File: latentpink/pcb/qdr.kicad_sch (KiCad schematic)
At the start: 2 parts, among them U2 XC7K160T-2FBG484C, U3 CY7C2245KV18-450BZXI

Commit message: Continued initial schematic capture
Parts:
- added C124, C125, C126, C127: 4.7 uF, azonenberg_pcb:EIA_0603_CAP_NOSILK, symbol device:C
- added C128, C129, C130, C131, C132, C133, C134, C135, C136, C137, C138, C139, C140, C141, C142, C143, C144, C145, C146, C147, C148, C149, C150, C151, C152, C153: 0.47 uF, azonenberg_pcb:EIA_0402_CAP_NOSILK, symbol device:C
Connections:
- net GND: now reaches U3.C4 (GND)
- net GND: now also U3.C8 (GND), U3.D4 (GND), U3.D5 (GND), U3.D6 (GND), U3.D7 (GND), U3.D8 (GND), U3.E5 (GND), U3.E6 (GND), U3.E7 (GND), U3.F6 (GND), U3.G6 (GND), U3.H6 (GND), U3.J6 (GND), U3.K6 (GND), U3.L5 (GND), U3.L6 (GND), U3.L7 (GND), U3.M4 (GND), U3.M5 (GND), U3.M6 (GND), U3.M7 (GND), U3.M8 (GND), U3.N4 (GND), U3.N8 (GND), C124.2, C125.2, C126.2, C127.2, C128.2, C129.2, C130.2, C131.2, C132.2, C133.2, C134.2, C135.2, C136.2, C137.2, C138.2, C139.2, C140.2, C141.2, C142.2, C143.2, C144.2, C145.2, C146.2, C147.2, C148.2, C149.2, C150.2, C151.2, C152.2, C153.2
- net 1V8_IO: now reaches U3.E4 (VDDQ)
- net 1V8_IO: now also U3.E8 (VDDQ), U3.F4 (VDDQ), U3.F8 (VDDQ), U3.G4 (VDDQ), U3.G8 (VDDQ), U3.H3 (VDDQ), U3.H4 (VDDQ), U3.H8 (VDDQ), U3.H9 (VDDQ), U3.J4 (VDDQ), U3.J8 (VDDQ), U3.K4 (VDDQ), U3.K8 (VDDQ), U3.L4 (VDDQ), U3.L8 (VDDQ), C126.1, C127.1, C128.1, C131.1, C132.1, C133.1, C136.1, C137.1, C138.1, C141.1, C142.1, C143.1, C146.1, C147.1, C148.1, C151.1, C152.1, C153.1
- net 1V8: now reaches U3.F5 (VDD)
- net 1V8: now also U3.F7 (VDD), U3.G5 (VDD), U3.G7 (VDD), U3.H5 (VDD), U3.H7 (VDD), U3.J5 (VDD), U3.J7 (VDD), U3.K5 (VDD), U3.K7 (VDD), C124.1, C125.1, C129.1, C130.1, C134.1, C135.1, C139.1, C140.1, C144.1, C145.1, C149.1, C150.1
- net QDR_WPS_N: now reaches U3.A4 (WPS_N)
- net QDR_WPS_N: now also U2.K16 (IO_0_14)
- net QDR_BWS_2_N: now reaches U3.A5 (BWS_2_N)
- net QDR_BWS_2_N: now also U2.AA15 (IO_L18N_T2_13)
- net QDR_BWS_1_N: now reaches U3.A7 (BWS_1_N)
- net QDR_BWS_1_N: now also U2.W19 (IO_12N_T1_MRCC_13)
- net QDR_D18: now reaches U3.B3 (D18)
- net QDR_D18: now also U2.Y18 (IO_L13P_T2_MRCC_13)
- net QDR_BWS_3_N: now reaches U3.B5 (BWS_3_N)
- net QDR_BWS_3_N: now also U2.U15 (IO_L24N_T3_13)
- net QDR_BWS_0_N: now reaches U3.B7 (BWS_0_N)
- net QDR_BWS_0_N: now also U2.U20 (IO_L6N_T0_VREF_13)
- net QDR_D17: now reaches U3.B9 (D17)
- net QDR_D17: now also U2.V19 (IO_L12P_T1_MRCC_13)
- net QDR_D27: now reaches U3.C1 (D27)
- net QDR_D27: now also U2.U16 (IO_L19P_T3_13)
- net QDR_D8: now reaches U3.C11 (D8)
- net QDR_D8: now also U2.T20 (IO_L6P_T0_13)
- net QDR_D19: now reaches U3.C3 (D19)
- net QDR_D19: now also U2.Y19 (IO_L13N_T2_MRCC_13)
- net QDR_D16: now reaches U3.C9 (D16)
- net QDR_D16: now also U2.W20 (IO_L11N_T1_SRCC_13)
- net QDR_D28: now reaches U3.D1 (D28)
- net QDR_D28: now also U2.V17 (IO_L19N_T3_VREF_13)
- net QDR_D15: now reaches U3.D10 (D15)
- net QDR_D15: now also U2.V20 (IO_L11P_T1_SRCC_13)
- net QDR_D7: now reaches U3.D11 (D7)
- net QDR_D7: now also U2.V18 (IO_L5N_T0_13)
- net QDR_D20: now reaches U3.D2 (D20)
- net QDR_D20: now also U2.W17 (IO_L14P_T2_SRCC_13)
- net QDR_D6: now reaches U3.E10 (D6)
- net QDR_D6: now also U2.U17 (IO_L5P_T0_13)
- net QDR_D29: now reaches U3.E2 (D29)
- net QDR_D29: now also U2.R16 (IO_L20P_T3_13)
- net QDR_D21: now reaches U3.F3 (D21)
- net QDR_D21: now also U2.Y17 (IO_L14N_T2_SRCC_13)
- net QDR_D14: now reaches U3.F9 (D14)
- net QDR_D14: now also U2.AB20 (IO_L10N_T1_13)
- net QDR_D30: now reaches U3.G1 (D30)
- net QDR_D30: now also U2.T16 (IO_L20N_T3_13)
- net QDR_D13: now reaches U3.G10 (D13)
- net QDR_D13: now also U2.AA19 (IO_L10_PT1_13)
- net QDR_D5: now reaches U3.G11 (D5)
- net QDR_D5: now also U2.W22 (IO_L4N_T0_13)
- net QDR_D22: now reaches U3.G2 (D22)
- net QDR_D22: now also U2.AB15 (IO_L16P_T2_13)
- net QDR_D31: now reaches U3.J1 (D31)
- net QDR_D31: now also U2.W14 (IO_L22P_T3_13)
- net QDR_D4: now reaches U3.J11 (D4)
- net QDR_D4: now also U2.W21 (IO_L4P_T0_13)
- net QDR_D23: now reaches U3.J3 (D23)
- net QDR_D23: now also U2.AB16 (IO_L16N_T2_13)
- net QDR_D12: now reaches U3.J9 (D12)
- net QDR_D12: now also U2.AB21 (IO_L8N_T1_13)
- net QDR_D3: now reaches U3.K10 (D3)
- net QDR_D3: now also U2.V22 (IO_L2N_T0_13)
- net QDR_D32: now reaches U3.K2 (D32)
- net QDR_D32: now also U2.Y14 (IO_L22N_T3_13)
- net QDR_D24: now reaches U3.L3 (D24)
- net QDR_D24: now also U2.AA16 (IO_L17P_T2_13)
- net QDR_D11: now reaches U3.L9 (D11)
- net QDR_D11: now also U2.AA20 (IO_L8P_T1_13)
- net QDR_D33: now reaches U3.M1 (D33)
- net QDR_D33: now also U2.V15 (IO_L23P_T3_13)
- net QDR_D2: now reaches U3.M11 (D2)
- net QDR_D2: now also U2.U22 (IO_L2P_T0_13)
- net QDR_D25: now reaches U3.M3 (D25)
- net QDR_D25: now also U2.AB17 (IO_L17N_T2_13)
- net QDR_D10: now reaches U3.M9 (D10)
- net QDR_D10: now also U2.Y22 (IO_L7N_T1_13)
- net QDR_D34: now reaches U3.N1 (D34)
- net QDR_D34: now also U2.W15 (IO_L23N_T3_13)
- net QDR_D9: now reaches U3.N10 (D9)
- net QDR_D9: now also U2.Y21 (IO_L7P_T1_13)
- net QDR_D1: now reaches U3.N11 (D1)
- net QDR_D1: now also U2.U21 (IO_L1N_T0_13)
- net QDR_D26: now reaches U3.N2 (D26)
- net QDR_D26: now also U2.AA14 (IO_L18P_T2_13)
- net QDR_D0: now reaches U3.P10 (D0)
- net QDR_D0: now also U2.T21 (IO_L1P_T0_13)
- net QDR_D35: now reaches U3.P2 (D35)
- net QDR_D35: now also U2.T15 (IO_L24P_T3_13)
- net QDR_CQ_N: now reaches U3.A1 (CQ_N)
- net QDR_CQ_N: now also U2.L20 (IO_L12N_T1_MRCC_14)
- net QDR_CQ_P: now reaches U3.A11 (CQ_P)
- net QDR_CQ_P: now also U2.L19 (IO_L12P_T1_MRCC_14)
- net QDR_RPS_N: now reaches U3.A8 (RPS_N)
- net QDR_RPS_N: now also U2.H18 (IO_L1P_T0_D00_MOSI_14)
- net QDR_QVLD: now reaches U3.P6 (QVLD)
- net QDR_QVLD: now also U2.H19 (IO_L1N_T0_D01_DIN_14)
- net QDR_A10: now reaches U2.E21 (IO_L7P_T1_D09_14)
- net QDR_A10: now also U3.P7 (A)
- net QDR_A11: now reaches U2.E22 (IO_L7N_T1_D10_14)
- net QDR_A11: now also U3.P8 (A)
- net QDR_A1: now reaches U2.F19 (IO_L2N_T0_D03_14)
- net QDR_A1: now also U3.B4 (A)
- net QDR_A5: now reaches U2.F20 (IO_L4N_T0_D05_14)
- net QDR_A5: now also U3.N5 (A)
- net QDR_A15: now reaches U2.F21 (IO_L9N_T1_DQS_D13_14)
- net QDR_A15: now also U3.R7 (A)
- net QDR_A0: now reaches U2.G18 (IO_L2P_T0_D02_14)
- net QDR_A0: now also U3.A9 (A)
- net QDR_A4: now reaches U2.G20 (IO_L4P_T0_D04_14)
- net QDR_A4: now also U3.C7 (A)
- net QDR_A14: now reaches U2.G21 (IO_L9P_T1_DQS_14)
- net QDR_A14: now also U3.R5 (A)
- net QDR_A13: now reaches U2.G22 (IO_L8N_T1_D12_14)
- net QDR_A13: now also U3.R4 (A)
- net QDR_A12: now reaches U2.H22 (IO_L8P_T1_D11_14)
- net QDR_A12: now also U3.R3 (A)
- net QDR_A3: now reaches U2.J19 (IO_L3N_T0_DQS_EMCCLK_14)
- net QDR_A3: now also U3.C5 (A)
- net QDR_A16: now reaches U2.J21 (IO_L10P_T1_D14_14)
- net QDR_A16: now also U3.R8 (A)
- net QDR_A17: now reaches U2.J22 (IO_L10N_T1_D15_14)
- net QDR_A17: now also U3.R9 (A)
- net QDR_A9: now reaches U2.K17 (IO_L6N_T0_D08_VREF_14)
- net QDR_A9: now also U3.P5 (A)
- net QDR_A2: now reaches U2.K18 (IO_L3P_T0_DQS_PUDC_B_14)
- net QDR_A2: now also U3.B8 (A)
- net QDR_A7: now reaches U2.K19 (IO_L5N_T0_D07_14)
- net QDR_A7: now also U3.N7 (A)
- net QDR_A8: now reaches U2.L16 (IO_L6P_T0_FCS_B_14)
- net QDR_A8: now also U3.P4 (A)
- net QDR_A6: now reaches U2.L18 (IO_L5P_T0_D06_14)
- net QDR_A6: now also U3.N6 (A)
- net QDR_A20: now reaches U2.M17 (IO_L14P_T2_SRCC_14)
- net QDR_A20: now also U3.A2 (NC/288M)
- net QDR_A19: now reaches U2.M18 (IO_L14N_T2_SRCC_14)
- net QDR_A19: now also U3.A10 (NC/144M)
- net QDR_SYSCLK_P: now reaches U2.N18 (IO_L13P_T2_MRCC_14)
- net QDR_SYSCLK_N: now reaches U2.N19 (IO_L13N_T2_MRCC_14)
- net QDR_A18: now reaches U2.N22 (IO_L15P_T2_DQS_RDWR_B_14)
- net QDR_A18: now also U3.A3 (NC/72M)
- net QDR_K_P: now reaches U2.AA21 (IO_L9P_T1_DQS_13)
- net QDR_K_P: now also U3.B6 (K)
- net QDR_K_N: now reaches U2.AB22 (IO_L9N_T1_DQS_13)
- net QDR_K_N: now also U3.A6 (K_N)
- no-connect marks 0 -> 8
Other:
- note added: "TODO: verify termination * C/A bus: external resistors to Vtt * D: ODT on QDR * Q: DCI inputs on FPGA"
- moved on the sheet: U2C, U2D, U2E, U3B, U3C

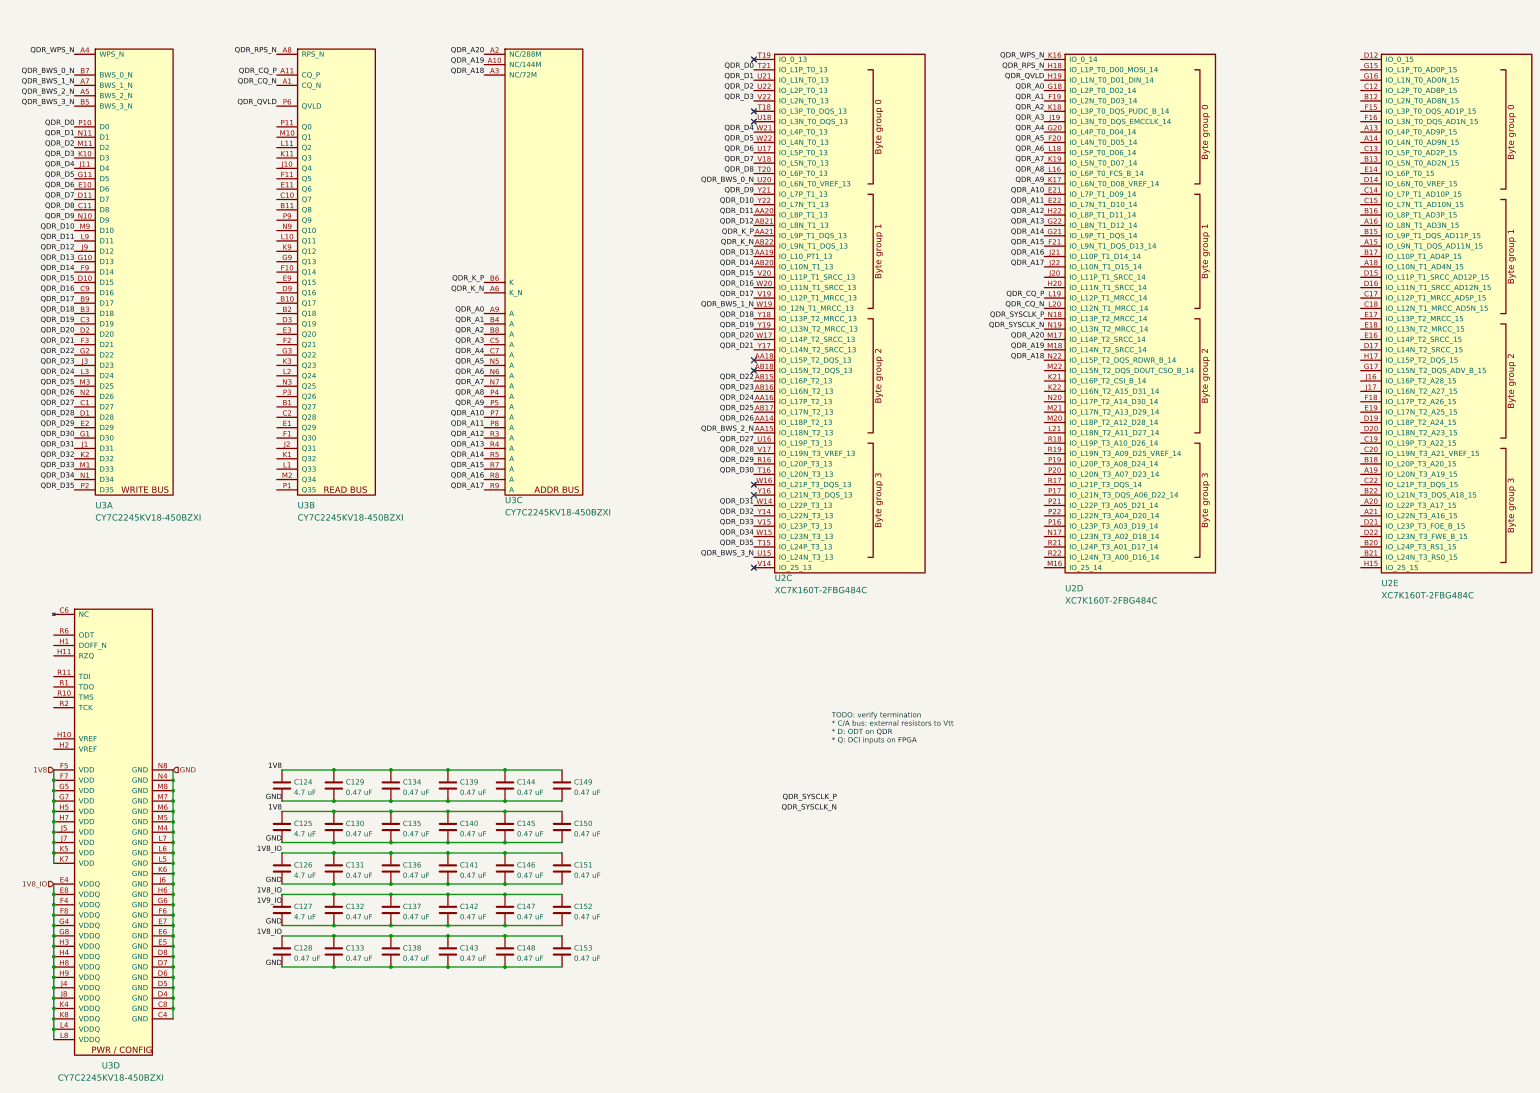
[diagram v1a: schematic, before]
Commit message: Continued work on schematic, mostly power supply and QDR
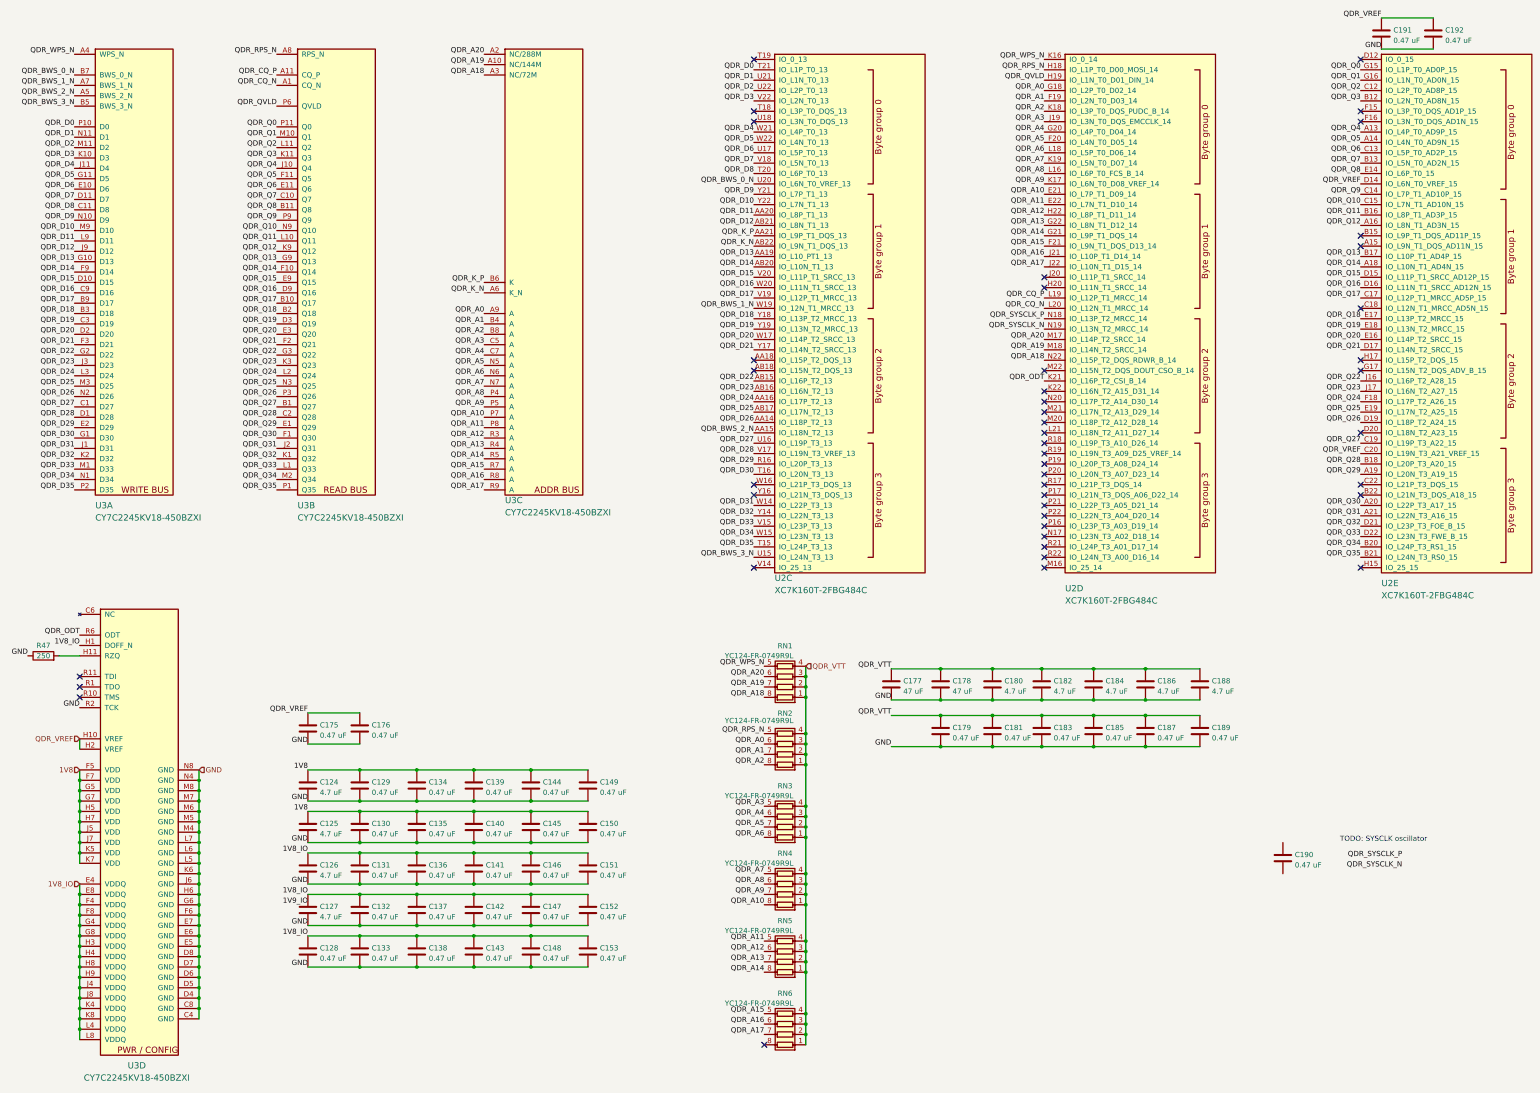
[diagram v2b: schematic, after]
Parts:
- added C175, C176, C179, C181, C183, C185, C187, C189, C190, C191, C192: 0.47 uF, azonenberg_pcb:EIA_0402_CAP_NOSILK, symbol device:C
- added C177, C178: 47 uF, symbol device:C
- added C180, C182, C184, C186, C188: 4.7 uF, azonenberg_pcb:EIA_0603_CAP_NOSILK, symbol device:C
- added R47: 250, symbol device:R
- added RN1, RN2, RN3, RN4, RN5, RN6: YC124-FR-0749R9L, symbol device:R_Pack04
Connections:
- net 1V8_IO: now also U3.H1 (DOFF_N)
- net GND: now also U3.R2 (TCK), C175.2, C176.2, C177.2, C178.2, C179.2, C180.2, C181.2, C182.2, C183.2, C184.2, C185.2, C186.2, C187.2, C188.2, C189.2, C191.2, C192.2, R47.1
- net QDR_A0: now also RN2.6 (R3.2)
- net QDR_A1: now also RN2.7 (R2.2)
- net QDR_A10: now also RN4.8 (R1.2)
- net QDR_A11: now also RN5.5 (R4.2)
- net QDR_A12: now also RN5.6 (R3.2)
- net QDR_A13: now also RN5.7 (R2.2)
- net QDR_A14: now also RN5.8 (R1.2)
- net QDR_A15: now also RN6.5 (R4.2)
- net QDR_A16: now also RN6.6 (R3.2)
- net QDR_A17: now also RN6.7 (R2.2)
- net QDR_A18: now also RN1.8 (R1.2)
- net QDR_A19: now also RN1.7 (R2.2)
- net QDR_A2: now also RN2.8 (R1.2)
- net QDR_A20: now also RN1.6 (R3.2)
- net QDR_A3: now also RN3.5 (R4.2)
- net QDR_A4: now also RN3.6 (R3.2)
- net QDR_A5: now also RN3.7 (R2.2)
- net QDR_A6: now also RN3.8 (R1.2)
- net QDR_A7: now also RN4.5 (R4.2)
- net QDR_A8: now also RN4.6 (R3.2)
- net QDR_A9: now also RN4.7 (R2.2)
- net QDR_RPS_N: now also RN2.5 (R4.2)
- net QDR_WPS_N: now also RN1.5 (R4.2)
- net QDR_VREF: now reaches U3.H10 (VREF)
- net QDR_VREF: now also U2.C20 (IO_L19N_T3_A21_VREF_15), U2.D14 (IO_L6N_T0_VREF_15), U3.H2 (VREF), C175.1, C176.1, C191.1, C192.1
- net at U3.H11 (RZQ): now also R47.2
- net QDR_ODT: now reaches U3.R6 (ODT)
- net QDR_ODT: now also U2.K21 (IO_L16P_T2_CSI_B_14)
- net QDR_Q4: now reaches U2.A13 (IO_L4P_T0_AD9P_15)
- net QDR_Q4: now also U3.J10 (Q4)
- net QDR_Q5: now reaches U2.A14 (IO_L4N_T0_AD9N_15)
- net QDR_Q5: now also U3.F11 (Q5)
- net QDR_Q12: now reaches U2.A16 (IO_L8N_T1_AD3N_15)
- net QDR_Q12: now also U3.K9 (Q12)
- net QDR_Q14: now reaches U2.A18 (IO_L10N_T1_AD4N_15)
- net QDR_Q14: now also U3.F10 (Q14)
- net QDR_Q29: now reaches U2.A19 (IO_L20N_T3_A19_15)
- net QDR_Q29: now also U3.E1 (Q29)
- net QDR_Q30: now reaches U2.A20 (IO_L22P_T3_A17_15)
- net QDR_Q30: now also U3.F1 (Q30)
- net QDR_Q31: now reaches U2.A21 (IO_L22N_T3_A16_15)
- net QDR_Q31: now also U3.J2 (Q31)
- net QDR_Q3: now reaches U2.B12 (IO_L2N_T0_AD8N_15)
- net QDR_Q3: now also U3.K11 (Q3)
- net QDR_Q7: now reaches U2.B13 (IO_L5N_T0_AD2N_15)
- net QDR_Q7: now also U3.C10 (Q7)
- net QDR_Q11: now reaches U2.B16 (IO_L8P_T1_AD3P_15)
- net QDR_Q11: now also U3.L10 (Q11)
- net QDR_Q13: now reaches U2.B17 (IO_L10P_T1_AD4P_15)
- net QDR_Q13: now also U3.G9 (Q13)
- net QDR_Q28: now reaches U2.B18 (IO_L20P_T3_A20_15)
- net QDR_Q28: now also U3.C2 (Q28)
- net QDR_Q34: now reaches U2.B20 (IO_L24P_T3_RS1_15)
- net QDR_Q34: now also U3.M2 (Q34)
- net QDR_Q35: now reaches U2.B21 (IO_L24N_T3_RS0_15)
- net QDR_Q35: now also U3.P1 (Q35)
- net QDR_Q2: now reaches U2.C12 (IO_L2P_T0_AD8P_15)
- net QDR_Q2: now also U3.L11 (Q2)
- net QDR_Q6: now reaches U2.C13 (IO_L5P_T0_AD2P_15)
- net QDR_Q6: now also U3.E11 (Q6)
- net QDR_Q9: now reaches U2.C14 (IO_L7P_T1_AD10P_15)
- net QDR_Q9: now also U3.P9 (Q9)
- net QDR_Q10: now reaches U2.C15 (IO_L7N_T1_AD10N_15)
- net QDR_Q10: now also U3.N9 (Q10)
- net QDR_Q17: now reaches U2.C17 (IO_L12P_T1_MRCC_AD5P_15)
- net QDR_Q17: now also U3.B10 (Q17)
- net QDR_Q27: now reaches U2.C19 (IO_L19P_T3_A22_15)
- net QDR_Q27: now also U3.B1 (Q27)
- net QDR_Q15: now reaches U2.D15 (IO_L11P_T1_SRCC_AD12P_15)
- net QDR_Q15: now also U3.E9 (Q15)
- net QDR_Q16: now reaches U2.D16 (IO_L11N_T1_SRCC_AD12N_15)
- net QDR_Q16: now also U3.D9 (Q16)
- net QDR_Q21: now reaches U2.D17 (IO_L14N_T2_SRCC_15)
- net QDR_Q21: now also U3.F2 (Q21)
- net QDR_Q26: now reaches U2.D19 (IO_L18P_T2_A24_15)
- net QDR_Q26: now also U3.P3 (Q26)
- net QDR_Q32: now reaches U2.D21 (IO_L23P_T3_FOE_B_15)
- net QDR_Q32: now also U3.K1 (Q32)
- net QDR_Q33: now reaches U2.D22 (IO_L23N_T3_FWE_B_15)
- net QDR_Q33: now also U3.L1 (Q33)
- net QDR_Q8: now reaches U2.E14 (IO_L6P_T0_15)
- net QDR_Q8: now also U3.B11 (Q8)
- net QDR_Q20: now reaches U2.E16 (IO_L14P_T2_SRCC_15)
- net QDR_Q20: now also U3.E3 (Q20)
- net QDR_Q18: now reaches U2.E17 (IO_L13P_T2_MRCC_15)
- net QDR_Q18: now also U3.B2 (Q18)
- net QDR_Q19: now reaches U2.E18 (IO_L13N_T2_MRCC_15)
- net QDR_Q19: now also U3.D3 (Q19)
- net QDR_Q25: now reaches U2.E19 (IO_L17N_T2_A25_15)
- net QDR_Q25: now also U3.N3 (Q25)
- net QDR_Q24: now reaches U2.F18 (IO_L17P_T2_A26_15)
- net QDR_Q24: now also U3.L2 (Q24)
- net QDR_Q0: now reaches U2.G15 (IO_L1P_T0_AD0P_15)
- net QDR_Q0: now also U3.P11 (Q0)
- net QDR_Q1: now reaches U2.G16 (IO_L1N_T0_AD0N_15)
- net QDR_Q1: now also U3.M10 (Q1)
- net QDR_Q22: now reaches U2.J16 (IO_L16P_T2_A28_15)
- net QDR_Q22: now also U3.G3 (Q22)
- net QDR_Q23: now reaches U2.J17 (IO_L16N_T2_A27_15)
- net QDR_Q23: now also U3.K3 (Q23)
- new net QDR_VTT: C177.1, C178.1, C179.1, C180.1, C181.1, C182.1, C183.1, C184.1, C185.1, C186.1, C187.1, C188.1, C189.1, RN1.1 (R1.1), RN1.2 (R2.1), RN1.3 (R3.1), RN1.4 (R4.1), RN2.1 (R1.1), RN2.2 (R2.1), RN2.3 (R3.1), RN2.4 (R4.1), RN3.1 (R1.1), RN3.2 (R2.1), RN3.3 (R3.1), RN3.4 (R4.1), RN4.1 (R1.1), RN4.2 (R2.1), RN4.3 (R3.1), RN4.4 (R4.1), RN5.1 (R1.1), RN5.2 (R2.1), RN5.3 (R3.1), RN5.4 (R4.1), RN6.1 (R1.1), RN6.2 (R2.1), RN6.3 (R3.1), RN6.4 (R4.1)
- no-connect marks 8 -> 45
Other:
- note added: "TODO: SYSCLK oscillator"
- note removed: "TODO: verify termination * C/A bus: external resistors to Vtt * D: ODT on QDR * Q: DCI inputs on FPGA"
- moved on the sheet: C124, C125, C126, C127, C128, C129, C130, C131, C132, C133, C134, C135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
